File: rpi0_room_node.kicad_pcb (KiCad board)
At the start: 2 copper layers, 65 x 30 mm, 34 parts, among them J1 Raspberry Pi, J2 Conn_01x03, J3 Conn_01x03, J4 Conn_01x03, Q1 PDTC123Y, U1 AP2210K-3.3, U2 TSOP382xx, U3 RFM69HCW

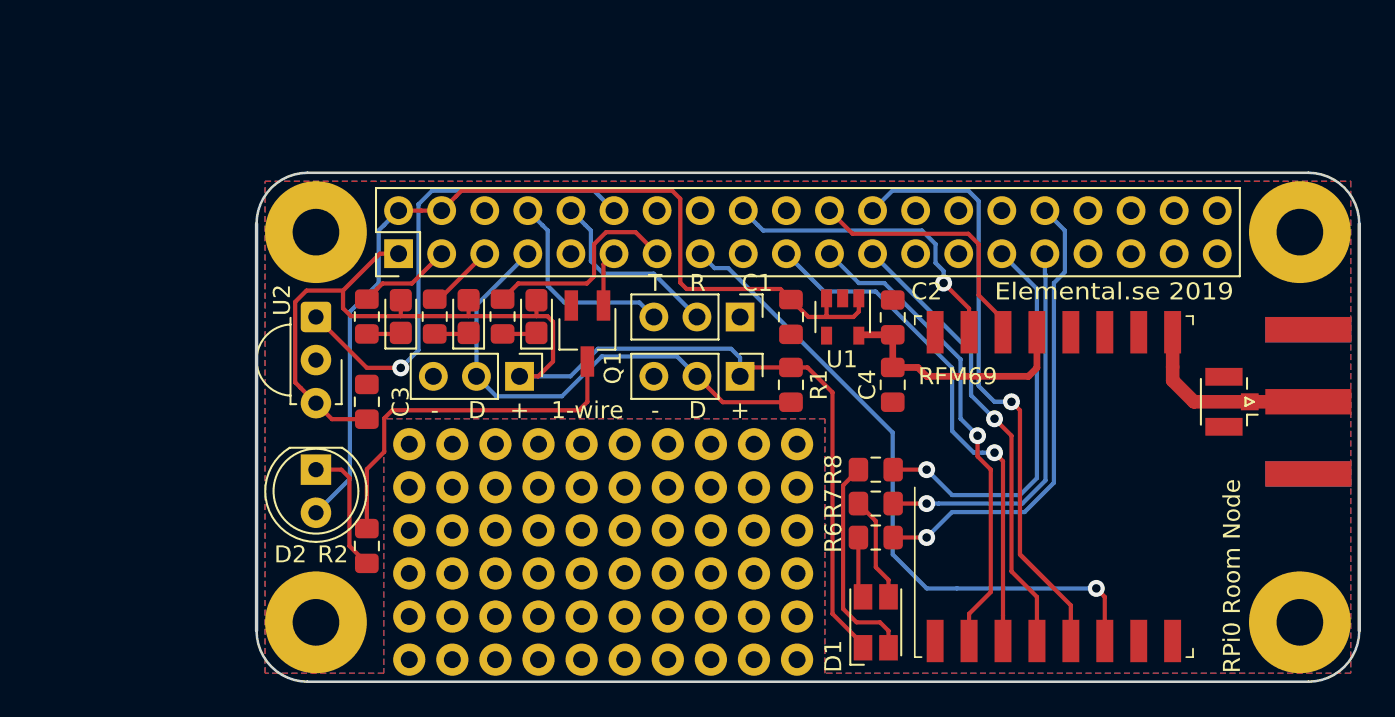
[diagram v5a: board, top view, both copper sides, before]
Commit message: Add test points, DIO 2
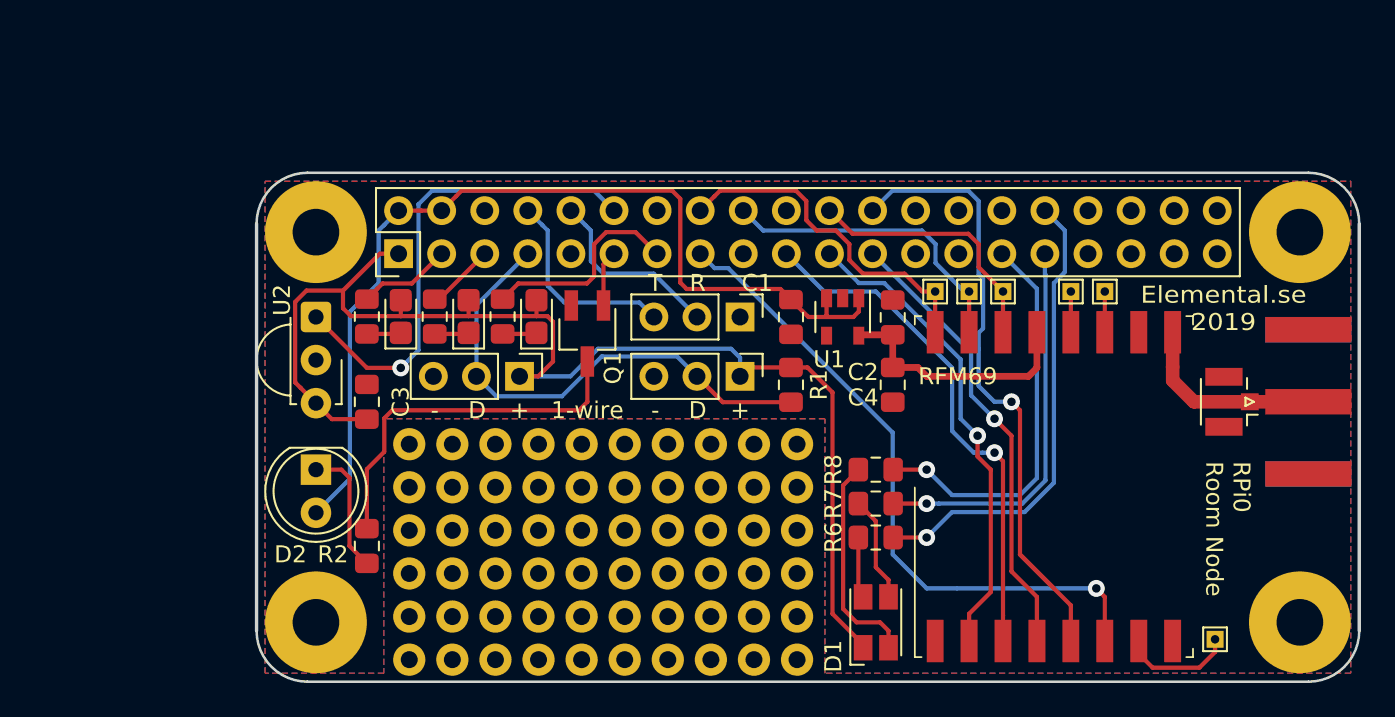
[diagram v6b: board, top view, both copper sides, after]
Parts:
- added TP1: TestPoint, TestPoint:TestPoint_THTPad_1.0x1.0mm_Drill0.5mm, F.Cu at (153.0, 124.0)
- added TP2: TestPoint, TestPoint:TestPoint_THTPad_1.0x1.0mm_Drill0.5mm, F.Cu at (144.5, 103.5)
- added TP3: TestPoint, TestPoint:TestPoint_THTPad_1.0x1.0mm_Drill0.5mm, F.Cu at (146.5, 103.5)
- added TP4: TestPoint, TestPoint:TestPoint_THTPad_1.0x1.0mm_Drill0.5mm, F.Cu at (136.5, 103.5)
- added TP5: TestPoint, TestPoint:TestPoint_THTPad_1.0x1.0mm_Drill0.5mm, F.Cu at (138.5, 103.5)
- added TP6: TestPoint, TestPoint:TestPoint_THTPad_1.0x1.0mm_Drill0.5mm, F.Cu at (140.5, 103.5)
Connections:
- J1 pad 16: Net-(J1-Pad16) -> /RFM_DIO2
- U3 pad 11: Net-(U3-Pad11) -> /RFM_DIO3
- U3 pad 12: Net-(U3-Pad12) -> /RFM_DIO4
- U3 pad 16: Net-(U3-Pad16) -> /RFM_DIO2
- U3 pad 7: Net-(U3-Pad7) -> /RFM_DIO5
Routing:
- net /RFM_DIO2: track 0.00 -> 20.4 mm
- net /RFM_DIO5: track 0.00 -> 6.72 mm
- net /RFM_DIO4: track 0.00 -> 2.40 mm
- net /RFM_DIO3: track 0.00 -> 2.40 mm
- net /RFM_DIO0: track 15.4 -> 16.2 mm
- net /RFM_DIO1: track 18.2 -> 18.3 mm, vias 1 -> 0
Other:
- rule solder_mask_min_width: 0.25 -> 0.1
- board text added: "0"
- board text added: "1"
- board text added: "2"
- board text added: "3"
- board text added: "4"
- board text added: "5"
- board text added: "RFM DIO"

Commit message: Add testpoint, clean up
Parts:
- added TP7: TestPoint, TestPoint:TestPoint_THTPad_1.0x1.0mm_Drill0.5mm, F.Cu at (132.0, 108.0)
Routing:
- net VDDA: track 15.7 -> 17.7 mm
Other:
- board text added: "RFM 3V3"
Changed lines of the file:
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@@
   (general
     (thickness 1.6)
-    (drawings 58)
-    (tracks 263)
+    (drawings 59)
+    (tracks 267)
     (zones 0)
-    (modules 40)
+    (modules 41)
     (nets 47)
   )
@@
     (tags "capacitor handsolder")
     (attr smd)
-    (fp_text reference C2 (at -3.225 -1.75 180) (layer F.SilkS)
+    (fp_text reference C2 (at -4.475 -1.75 180) (layer F.SilkS)
       (effects (font (size 1 1) (thickness 0.15)))
     )
@@
     (tags "capacitor handsolder")
     (attr smd)
-    (fp_text reference C4 (at 0.75 1.75) (layer F.SilkS)
+    (fp_text reference C4 (at 2 1.75) (layer F.SilkS)
       (effects (font (size 1 1) (thickness 0.15)))
     )
@@
       (net 27 /RFM_DIO0))
   )
+  (module TestPoint:TestPoint_THTPad_1.0x1.0mm_Drill0.5mm (layer F.Cu)
+    (at 132 108)
+    (descr "THT rectangular pad as test Point, square 1.0mm side length, hole diameter 0.5mm")
+    (tags "test point THT pad rectangle square")
+    (attr virtual)
+    (fp_text reference TP7 (at 0 -1.448) (layer F.SilkS) hide
+      (effects (font (size 1 1) (thickness 0.15)))
+    )
+    (fp_text value TestPoint (at 0 1.55) (layer F.Fab)
+      (effects (font (size 1 1) (thickness 0.15)))
+    )
+    (fp_text user %R (at 0 -1.45) (layer F.Fab)
+      (effects (font (size 1 1) (thickness 0.15)))
+    )
+    (fp_line (start -0.7 -0.7) (end 0.7 -0.7) (layer F.SilkS) (width 0.12))
+    (fp_line (start 0.7 -0.7) (end 0.7 0.7) (layer F.SilkS) (width 0.12))
+    (fp_line (start 0.7 0.7) (end -0.7 0.7) (layer F.SilkS) (width 0.12))
+    (fp_line (start -0.7 0.7) (end -0.7 -0.7) (layer F.SilkS) (width 0.12))
+    (fp_line (start -1 -1) (end 1 -1) (layer F.CrtYd) (width 0.05))
+    (fp_line (start -1 -1) (end -1 1) (layer F.CrtYd) (width 0.05))
+    (fp_line (start 1 1) (end 1 -1) (layer F.CrtYd) (width 0.05))
+    (fp_line (start 1 1) (end -1 1) (layer F.CrtYd) (width 0.05))
+    (pad 1 thru_hole rect (at 0 0) (size 1 1) (drill 0.5) (layers *.Cu *.Mask)
+      (net 26 VDDA))
+  )
+  (gr_text "RFM 3V3" (at 132 112 90) (layer B.SilkS)
+    (effects (font (size 1 1) (thickness 0.2)) (justify mirror))
+  )
   (gr_line (start 147.5 107.5) (end 147.5 102.5) (layer B.SilkS) (width 0.2))
   (gr_line (start 135.5 107.5) (end 147.5 107.5) (layer B.SilkS) (width 0.2))
@@
   )
   (gr_line (start 113.5 108.5) (end 118.5 108.5) (layer B.SilkS) (width 0.2))
-  (gr_line (start 131.5 110) (end 130.5 110) (layer B.SilkS) (width 0.2))
-  (gr_line (start 131.5 107) (end 131.5 110) (layer B.SilkS) (width 0.2))
-  (gr_line (start 130.5 107) (end 131.5 107) (layer B.SilkS) (width 0.2))
-  (gr_line (start 131.5 106.5) (end 130.5 106.5) (layer B.SilkS) (width 0.2))
-  (gr_line (start 131.5 103.5) (end 131.5 106.5) (layer B.SilkS) (width 0.2))
-  (gr_line (start 131 103.5) (end 131.5 103.5) (layer B.SilkS) (width 0.2))
+  (gr_line (start 131 110) (end 130.5 110) (layer B.SilkS) (width 0.2))
+  (gr_line (start 131 107) (end 131 110) (layer B.SilkS) (width 0.2))
+  (gr_line (start 130.5 107) (end 131 107) (layer B.SilkS) (width 0.2))
+  (gr_line (start 131 106.5) (end 130.5 106.5) (layer B.SilkS) (width 0.2))
+  (gr_line (start 131 103.5) (end 131 106.5) (layer B.SilkS) (width 0.2))
+  (gr_line (start 131 103.5) (end 131 103.5) (layer B.SilkS) (width 0.2))
   (gr_line (start 130.5 103.5) (end 131 103.5) (layer B.SilkS) (width 0.2))
   (gr_text serial (at 126.5 105) (layer B.SilkS)
@@
   (segment (start 122.46 108.5) (end 121.284999 107.324999) (width 0.25) (layer B.Cu) (net 4))
   (segment (start 110.635001 109.675001) (end 114.5 109.675001) (width 0.25) (layer B.Cu) (net 4))
-  (segment (start 116.95 101.89) (end 117.57 101.27) (width 0.25) (layer F.Cu) (net 5))
-  (segment (start 116.95 104.325) (end 116.95 101.89) (width 0.25) (layer F.Cu) (net 5))
+  (segment (start 116.95 103.092081) (end 116.95 103.5) (width 0.25) (layer F.Cu) (net 5))
+  (segment (start 117.57 102.472081) (end 116.95 103.092081) (width 0.25) (layer F.Cu) (net 5))
+  (segment (start 117.57 101.27) (end 117.57 102.472081) (width 0.25) (layer F.Cu) (net 5))
+  (segment (start 116.95 104.325) (end 116.95 103.5) (width 0.25) (layer F.Cu) (net 5))
   (segment (start 106.045001 98.355997) (end 106.045001 106.954999) (width 0.25) (layer B.Cu) (net 6))
   (segment (start 106.845999 97.554999) (end 106.045001 98.355997) (width 0.25) (layer B.Cu) (net 6))
@@
   (segment (start 141.5 119) (end 144.5 122) (width 0.25) (layer F.Cu) (net 11))
   (segment (start 141.5 119) (end 143.5 121) (width 0.25) (layer F.Cu) (net 11))
-  (segment (start 139.325001 102.739999) (end 139.325001 105.674999) (width 0.25) (layer B.Cu) (net 11))
   (segment (start 139.065001 98.165999) (end 139.065001 102.479999) (width 0.25) (layer B.Cu) (net 11))
-  (segment (start 139.065001 102.479999) (end 139.325001 102.739999) (width 0.25) (layer B.Cu) (net 11))
   (segment (start 139.065 105.935) (end 139.065001 106.888591) (width 0.25) (layer B.Cu) (net 11))
-  (segment (start 139.325001 105.674999) (end 139.065 105.935) (width 0.25) (layer B.Cu) (net 11))
   (segment (start 139.065001 106.888591) (end 139.065001 109.065001) (width 0.25) (layer B.Cu) (net 11))
+  (segment (start 139.065001 102.479999) (end 139.5 102.914998) (width 0.25) (layer B.Cu) (net 11))
+  (segment (start 139.5 105.5) (end 139.065 105.935) (width 0.25) (layer B.Cu) (net 11))
+  (segment (start 139.5 102.914998) (end 139.5 105.5) (width 0.25) (layer B.Cu) (net 11))
   (segment (start 131.975 121.225) (end 132.25 121.5) (width 0.25) (layer F.Cu) (net 21))
   (segment (start 131.975 118) (end 131.975 121.225) (width 0.25) (layer F.Cu) (net 21))
@@
   (segment (start 142 108.5) (end 142.5 108) (width 0.4) (layer F.Cu) (net 26))
   (segment (start 135.475 107.975) (end 134 107.975) (width 0.4) (layer F.Cu) (net 26))
+  (segment (start 133.975 108) (end 134 107.975) (width 0.25) (layer F.Cu) (net 26))
+  (segment (start 132 108) (end 133.975 108) (width 0.25) (layer F.Cu) (net 26))
   (segment (start 138.454001 100.094999) (end 139.065001 100.705999) (width 0.25) (layer F.Cu) (net 27))
   (segment (start 131.634999 100.094999) (end 138.454001 100.094999) (width 0.25) (layer F.Cu) (net 27))
@@
   (via (at 136 118) (size 1) (drill 0.5) (layers F.Cu B.Cu) (net 41))
   (segment (start 134.025 118) (end 136 118) (width 0.25) (layer F.Cu) (net 41))
-  (segment (start 137.5 116.5) (end 136 118) (width 0.25) (layer B.Cu) (net 41))
-  (segment (start 144.145001 99.905001) (end 144.145001 102.354999) (width 0.25) (layer B.Cu) (net 41))
-  (segment (start 144.145001 102.354999) (end 143.5 103) (width 0.25) (layer B.Cu) (net 41))
-  (segment (start 143.5 103) (end 143.5 114.77282) (width 0.25) (layer B.Cu) (net 41))
-  (segment (start 142.97 98.73) (end 144.145001 99.905001) (width 0.25) (layer B.Cu) (net 41))
-  (segment (start 143.5 114.77282) (end 141.77282 116.5) (width 0.25) (layer B.Cu) (net 41))
-  (segment (start 141.77282 116.5) (end 137.5 116.5) (width 0.25) (layer B.Cu) (net 41))
+  (segment (start 144.145001 99.905001) (end 142.97 98.73) (width 0.25) (layer B.Cu) (net 41))
+  (segment (start 136 118) (end 137.5 116.5) (width 0.25) (layer B.Cu) (net 41))
+  (segment (start 144.145001 102) (end 144.145001 99.905001) (width 0.25) (layer B.Cu) (net 41))
+  (segment (start 137.5 116.5) (end 141.77282 116.5) (width 0.25) (layer B.Cu) (net 41))
+  (segment (start 141.77282 116.5) (end 143.5 114.77282) (width 0.25) (layer B.Cu) (net 41))
+  (segment (start 143.5 102.645001) (end 144.145001 102) (width 0.25) (layer B.Cu) (net 41))
+  (segment (start 143.5 114.77282) (end 143.5 102.645001) (width 0.25) (layer B.Cu) (net 41))
   (segment (start 150.5 107.95) (end 150.5 105.9) (width 0.8) (layer F.Cu) (net 42))
   (segment (start 150.5 108.745002) (end 150.5 107.95) (width 0.8) (layer F.Cu) (net 42))
